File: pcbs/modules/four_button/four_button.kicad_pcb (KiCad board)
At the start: 2 copper layers, 25.5 x 32 mm, 10 parts, among them SW1 SW_Push, SW2 SW_Push, SW3 SW_Push, SW4 SW_Push

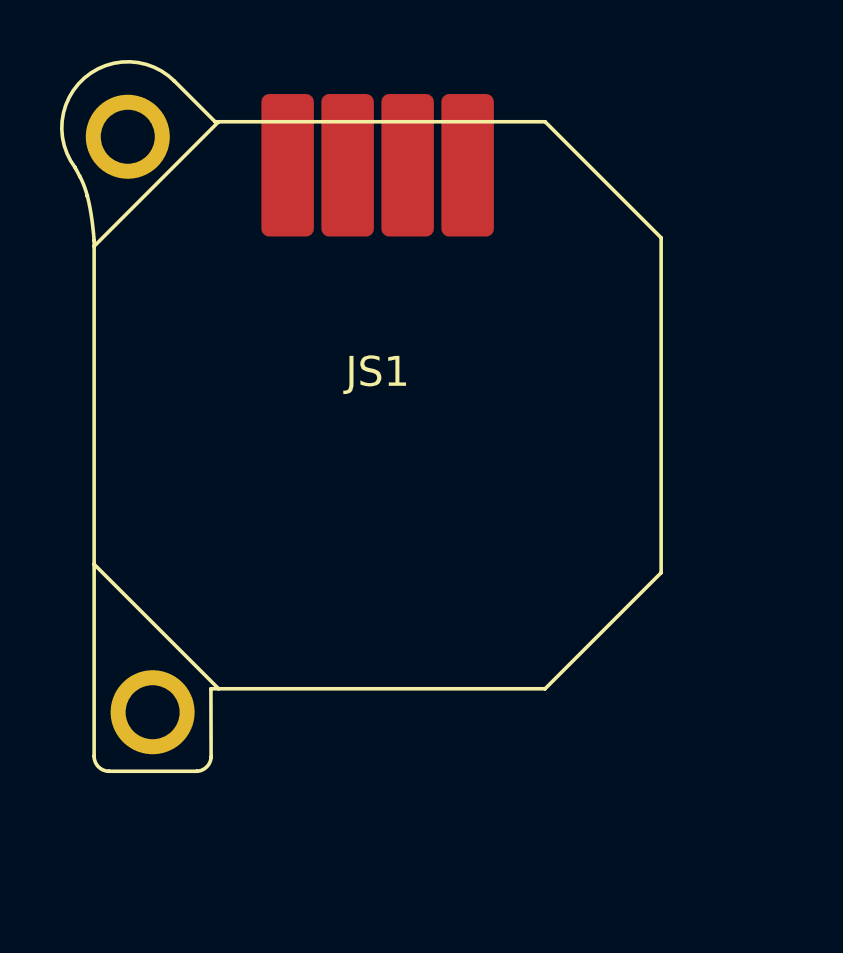
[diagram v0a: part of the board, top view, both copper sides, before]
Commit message: removed joystick from four button
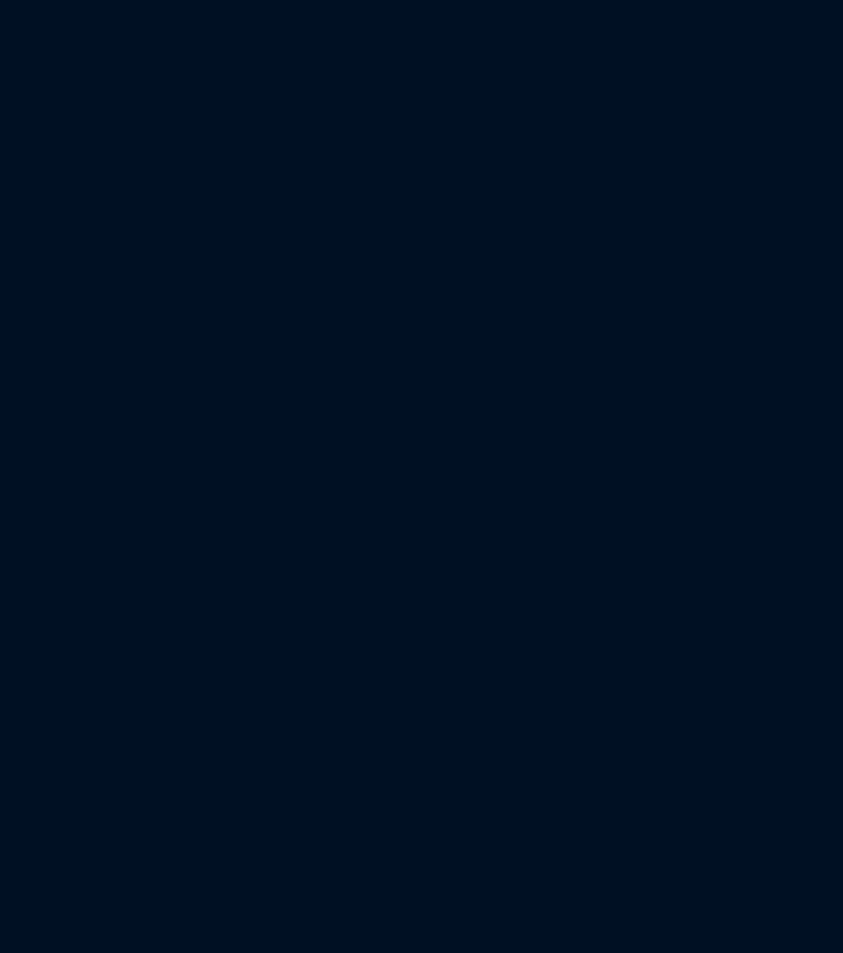
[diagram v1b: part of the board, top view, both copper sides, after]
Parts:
- removed JS1: joystick_analog, PCM_marbastlib-xp-various:PNT_psp1000
